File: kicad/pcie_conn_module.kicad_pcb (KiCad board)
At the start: 2 copper layers, 119.9 x 64.4 mm, 1 part, among them P1 pcie_1x_edge

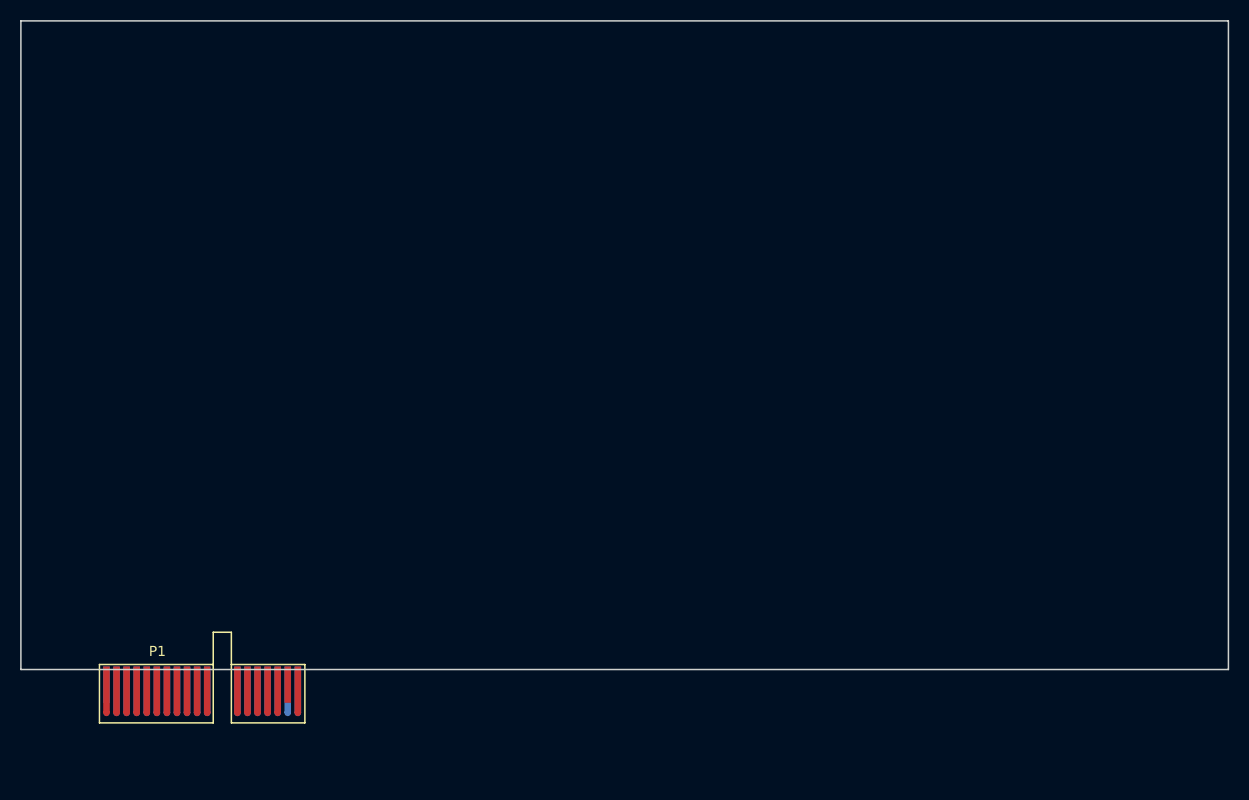
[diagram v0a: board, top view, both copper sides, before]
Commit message: add mux & eeprom
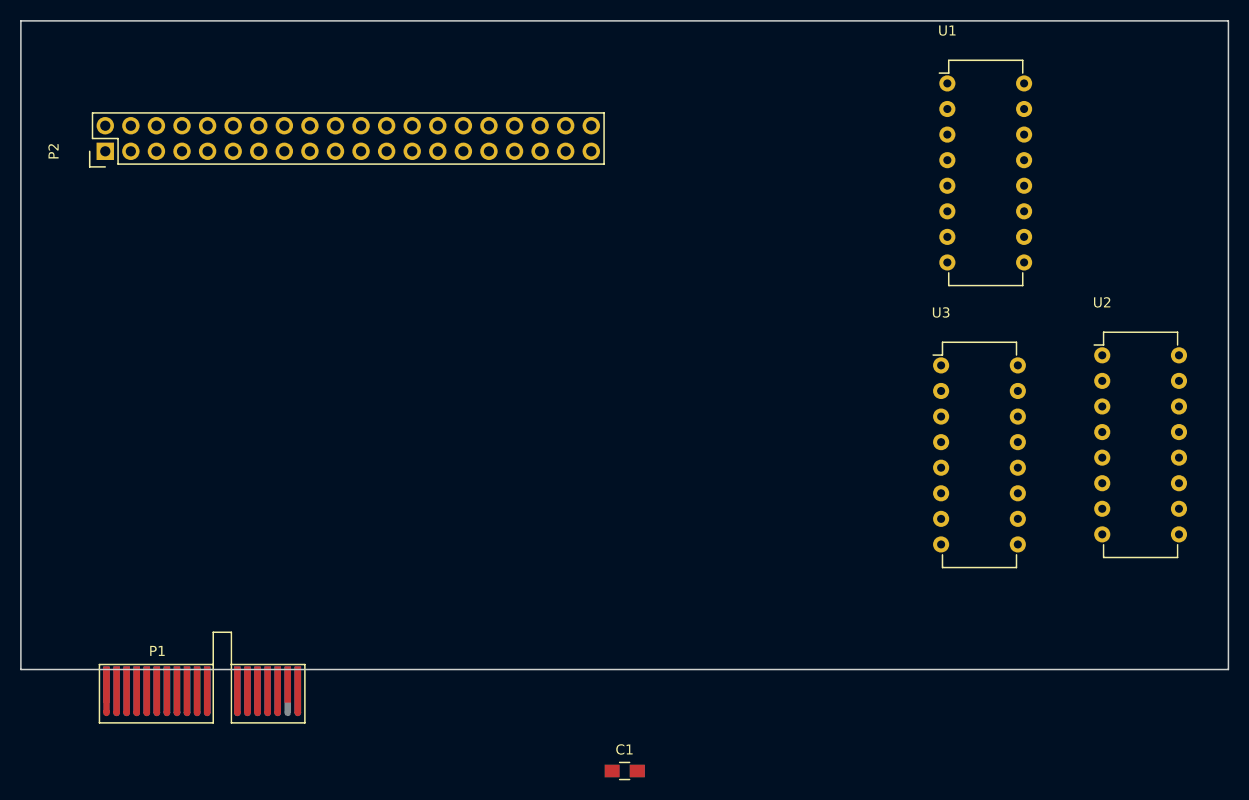
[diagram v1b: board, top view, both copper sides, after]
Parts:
- added C1: C_Small, Capacitors_SMD:C_0805_HandSoldering, F.Cu at (110.0, 160.1)
- added P2: CONN_02X20, Pin_Headers:Pin_Header_Straight_2x20, F.Cu at (58.4, 98.5)
- added U1: 74LS257, Housings_DIP:DIP-16_W7.62mm, F.Cu at (142.0, 91.8)
- added U2: 74LS157, Housings_DIP:DIP-16_W7.62mm, F.Cu at (157.4, 118.8)
- added U3: 74LS157, Housings_DIP:DIP-16_W7.62mm, F.Cu at (141.4, 119.8)
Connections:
- net Net-(P1-PadA10) renamed /Sclk_out
- net Net-(P1-PadA11) renamed /LRclk_out
- net Net-(P1-PadA12) renamed /I2S0_out
- net Net-(P1-PadA13) renamed /I2S1_out
- net Net-(P1-PadA14) renamed /I2S2_out
- net Net-(P1-PadA15) renamed /I2S3_out
- net Net-(P1-PadA7) renamed /SDA
- net Net-(P1-PadA9) renamed /Mclk_out
- net Net-(P1-PadB1) renamed /A0
- net Net-(P1-PadB2) renamed /A1
- net Net-(P1-PadB3) renamed /A2
- net Net-(P1-PadB7) renamed /SCL
- P1 pad A16: Net-(P1-PadA16) -> GND
- P1 pad A17: Net-(P1-PadA17) -> +3V3
- P1 pad A5: Net-(P1-PadA5) -> +3V3
- P1 pad A8: Net-(P1-PadA8) -> GND
- P1 pad B10: Net-(P1-PadB10) -> /Sclk_in
- P1 pad B11: Net-(P1-PadB11) -> /LRclk_in
- P1 pad B12: Net-(P1-PadB12) -> /I2S0_in
- P1 pad B13: Net-(P1-PadB13) -> /I2S1_in
- P1 pad B14: Net-(P1-PadB14) -> /I2S2_in
- P1 pad B15: Net-(P1-PadB15) -> /I2S3_in
- P1 pad B16: Net-(P1-PadB16) -> GND
- P1 pad B17: Net-(P1-PadB17) -> +3V3
- P1 pad B4: Net-(P1-PadB4) -> GND
- P1 pad B5: Net-(P1-PadB5) -> +3V3
- P1 pad B8: Net-(P1-PadB8) -> GND
- P1 pad B9: Net-(P1-PadB9) -> /Mclk_in

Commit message: first draft schematic
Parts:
- removed U3: 74LS157, Housings_DIP:DIP-16_W7.62mm
- added C2: C_Small, Capacitors_SMD:C_0805_HandSoldering, F.Cu at (84.2, 109.0)
- added C3: C_Small, Capacitors_SMD:C_0805_HandSoldering, F.Cu at (102.2, 109.0)
- added P3: CONN_01X03, Pin_Headers:Pin_Header_Straight_1x03, F.Cu at (71.5, 119.0)
- added P4: CONN_01X08, Pin_Headers:Pin_Header_Straight_1x08, F.Cu at (53.0, 132.7)
- added P5: CONN_01X18, Pin_Headers:Pin_Header_Straight_1x18, F.Cu at (62.0, 141.5)
- added P6: CONN_01X03, Pin_Headers:Pin_Header_Straight_1x03, F.Cu at (121.5, 92.0)
- added P7: CONN_02X20, Pin_Headers:Pin_Header_Straight_2x20, F.Cu at (61.8, 94.5)
- added R1: 10k, Resistors_SMD:R_0805_HandSoldering, F.Cu at (91.0, 122.0)
- added U4: PCA9500, Housings_SSOP:TSSOP-16_4.4x5mm_Pitch0.65mm, F.Cu at (62.8, 121.5)
- P2: value CONN_02X20 -> CONN_01X18; footprint Pin_Headers:Pin_Header_Straight_2x20 -> Pin_Headers:Pin_Header_Straight_1x18
- U1: value 74LS257 -> 74HCT157; footprint Housings_DIP:DIP-16_W7.62mm -> Housings_SOIC:SOIC-16_3.9x9.9mm_Pitch1.27mm
- U2: value 74LS157 -> 74HCT157; footprint Housings_DIP:DIP-16_W7.62mm -> Housings_SOIC:SOIC-16_3.9x9.9mm_Pitch1.27mm
- moved C1 66.3 mm to (62.2, 114.0)
- moved U1 64.5 mm to (84.0, 120.0)
- moved U2 55.4 mm to (102.0, 120.0)
- moved P2 33.7 mm to (62.0, 132.0)
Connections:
- net Net-(U1-Pad10) renamed /LRclk_mod
- net Net-(U1-Pad3) renamed /Mclk_mod
- net Net-(U1-Pad6) renamed /Sclk_mod
- net Net-(U2-Pad10) renamed /I2S2_mod
- net Net-(U2-Pad13) renamed /I2S3_mod
- net Net-(U2-Pad6) renamed /I2S1_mod
- P2 pad 1: Net-(P2-Pad1) -> /A0
- P2 pad 10: Net-(P2-Pad10) -> /Sclk_in
- P2 pad 11: Net-(P2-Pad11) -> /LRclk_in
- P2 pad 12: Net-(P2-Pad12) -> /I2S0_in
- P2 pad 13: Net-(P2-Pad13) -> /I2S1_in
- P2 pad 14: Net-(P2-Pad14) -> /I2S2_in
- P2 pad 15: Net-(P2-Pad15) -> /I2S3_in
- P2 pad 16: Net-(P2-Pad16) -> GND
- P2 pad 17: Net-(P2-Pad17) -> +3V3
- P2 pad 18: Net-(P2-Pad18) -> Net-(P1-PadB18)
- P2 pad 2: Net-(P2-Pad2) -> /A1
- P2 pad 3: Net-(P2-Pad3) -> /A2
- P2 pad 4: Net-(P2-Pad4) -> GND
- P2 pad 5: Net-(P2-Pad5) -> +3V3
- P2 pad 6: Net-(P2-Pad6) -> Net-(P1-PadB6)
- P2 pad 7: Net-(P2-Pad7) -> /SCL
- P2 pad 8: Net-(P2-Pad8) -> GND
- P2 pad 9: Net-(P2-Pad9) -> /Mclk_in
- U1 pad 1: Net-(U1-Pad1) -> Net-(P4-Pad1)
- U1 pad 11: Net-(U1-Pad11) -> /LRclk_in
- U1 pad 13: Net-(U1-Pad13) -> GND
- U1 pad 14: Net-(U1-Pad14) -> GND
- U1 pad 15: Net-(U1-Pad15) -> GND
- U1 pad 16: VCC -> +3V3
- U1 pad 2: Net-(U1-Pad2) -> /Mclk_in
- U1 pad 4: Net-(U1-Pad4) -> /Mclk_out
- U1 pad 5: Net-(U1-Pad5) -> /Sclk_in
- U1 pad 7: Net-(U1-Pad7) -> /Sclk_out
- U1 pad 9: Net-(U1-Pad9) -> /LRclk_out
- U2 pad 1: Net-(U2-Pad1) -> Net-(P4-Pad1)
- U2 pad 11: Net-(U2-Pad11) -> /I2S2_in
- U2 pad 12: Net-(U2-Pad12) -> /I2S3_out
- U2 pad 14: /LRclk_in -> /I2S3_in
- U2 pad 15: Net-(U2-Pad15) -> GND
- U2 pad 16: VCC -> +3V3
- U2 pad 2: /Mclk_in -> /I2S0_in
- U2 pad 3: Net-(U2-Pad3) -> /I2S0_mod
- U2 pad 4: Net-(U2-Pad4) -> /I2S0_out
- U2 pad 5: /Sclk_in -> /I2S1_in
- U2 pad 7: Net-(U2-Pad7) -> /I2S1_out
- U2 pad 9: Net-(U2-Pad9) -> /I2S2_out
